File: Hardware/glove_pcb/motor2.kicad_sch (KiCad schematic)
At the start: 22 parts, among them J8 Conn_01x02, U12 DRV8876PWPR

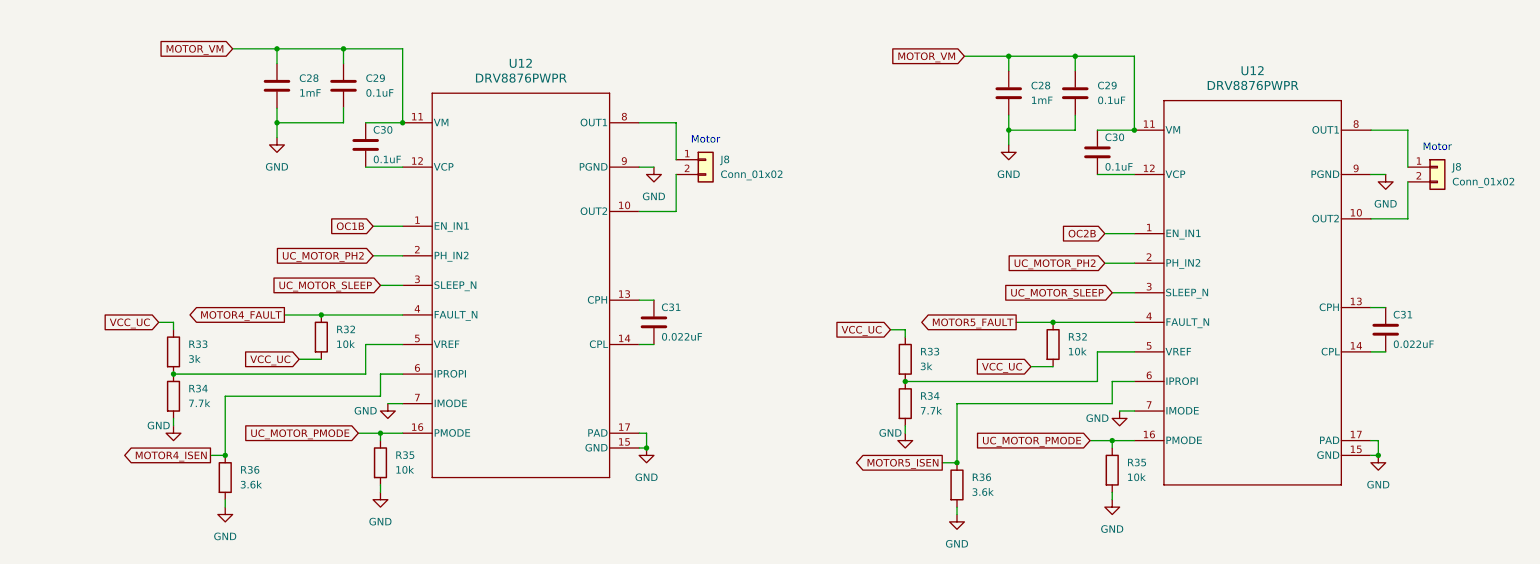
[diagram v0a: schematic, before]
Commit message: Add titles to pages and reannotate
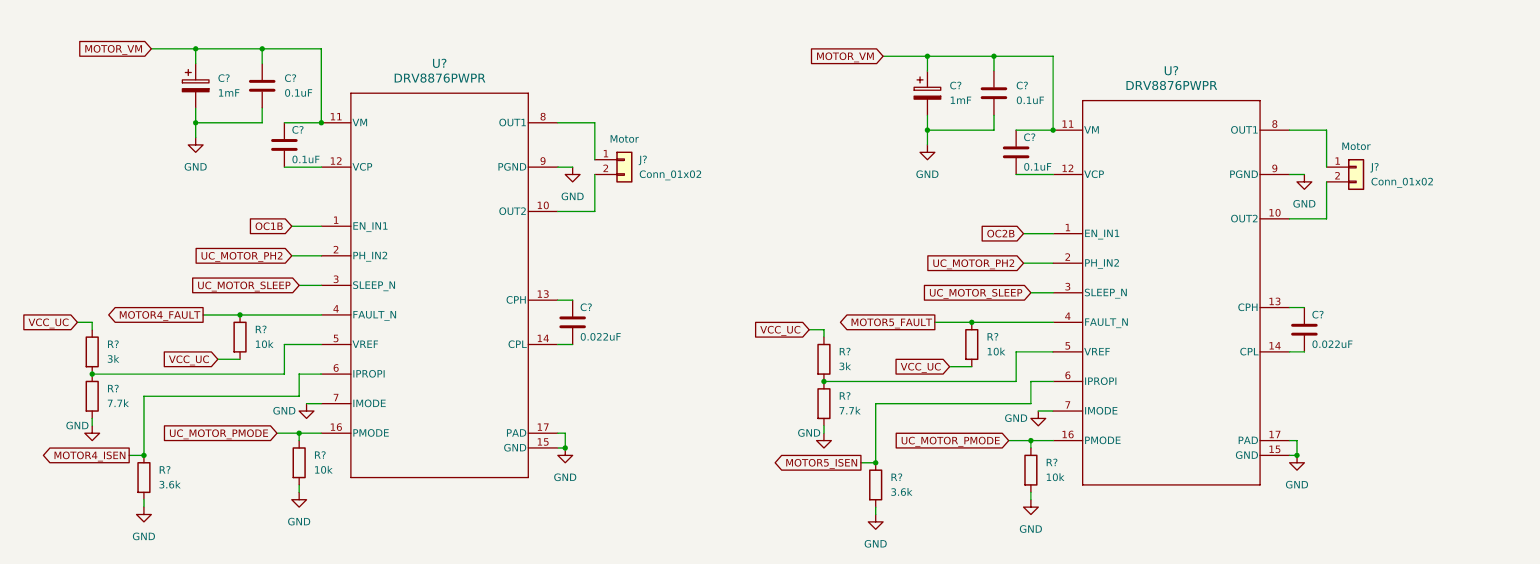
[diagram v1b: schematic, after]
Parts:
- C? (x2): renamed from C28; symbol Device:C -> Device:C_Polarized
- renumbered C30 to C?, C29 to C?, C31 to C?, J8 to J?, R36 to R?, R35 to R?, R34 to R?, R32 to R?, R33 to R?, U12 to U?
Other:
- company: (none) -> COEN 490 Team 15
- title: (none) -> Motor Drivers (2/2)
- moved on the sheet: C?, J?, R?, U?

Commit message: Finalize schematic for real this time
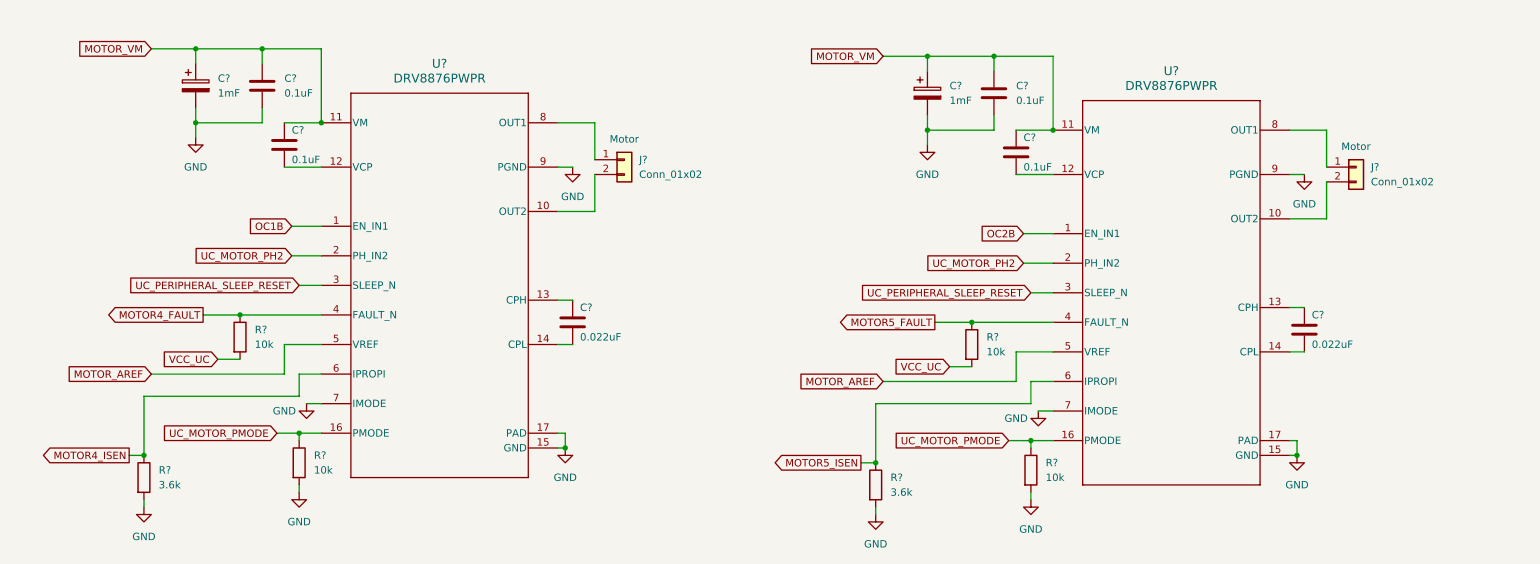
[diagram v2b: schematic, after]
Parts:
- removed R? (x2): 7.7k, symbol Device:R
- removed R? (x2): 3k, symbol Device:R
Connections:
- net MOTOR_AREF: now reaches U?.5 (VREF)
- net MOTOR_AREF: now also U?.5 (VREF)
- net UC_MOTOR_SLEEP renamed UC_PERIPHERAL_SLEEP_RESET

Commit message: Added Footprints
I Added footprints for every components in PCB
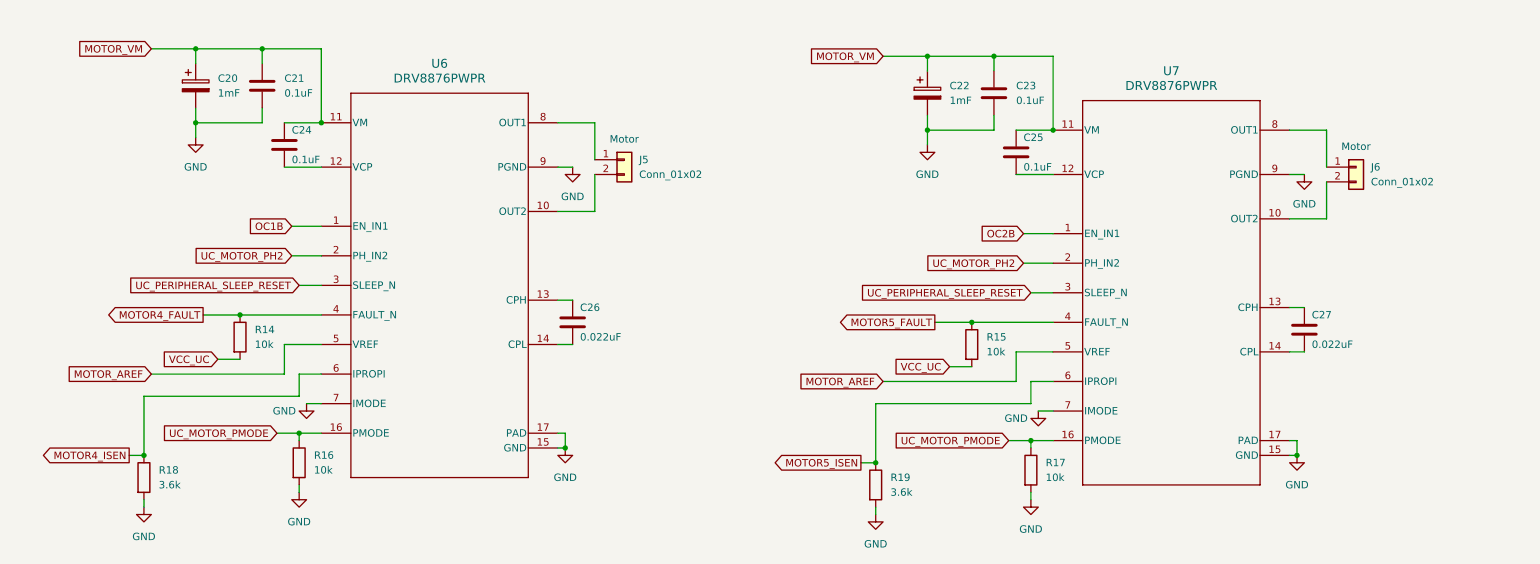
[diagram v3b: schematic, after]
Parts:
- C20, C22: renamed from C?; footprint (none) -> Capacitor_THT:CP_Radial_D10.0mm_P5.00mm
- C21, C23, C24, C25, C26, C27: renamed from C?; footprint (none) -> Capacitor_SMD:C_0603_1608Metric_Pad1.08x0.95mm_HandSolder
- J5, J6: renamed from J?; footprint (none) -> Connector_Molex:Molex_Micro-Fit_3.0_43650-0215_1x02_P3.00mm_Vertical
- R14, R15, R16, R17, R18, R19: renamed from R?; footprint (none) -> Resistor_SMD:R_0805_2012Metric_Pad1.20x1.40mm_HandSolder
- gave numbers to parts that had none: 2

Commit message: Made most of changes from meeting
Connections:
- net MOTOR_VM renamed +12V
- net VCC_UC renamed +5V
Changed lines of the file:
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@@
-    )
-  )
-  (global_label "VCC_UC" (shape input) (at 179.07 82.55 180) (fields_autoplaced)
-    (effects (font (size 1.27 1.27)) (justify right))
-    (property "Intersheetrefs" "${INTERSHEET_REFS}" (at 168.8881 82.55 0)
-      (effects (font (size 1.27 1.27)) (justify right) hide)
     )
   )
@@
     )
   )
-  (global_label "MOTOR_VM" (shape input) (at 41.91 27.94 180) (fields_autoplaced)
-    (effects (font (size 1.27 1.27)) (justify right))
-    (property "Intersheetrefs" "${INTERSHEET_REFS}" (at 29.0672 27.94 0)
-      (effects (font (size 1.27 1.27)) (justify right) hide)
-    )
-  )
   (global_label "UC_MOTOR_PH2" (shape input) (at 191.77 64.77 180) (fields_autoplaced)
     (effects (font (size 1.27 1.27)) (justify right))
@@
     )
   )
-  (global_label "MOTOR_VM" (shape input) (at 167.64 29.21 180) (fields_autoplaced)
-    (effects (font (size 1.27 1.27)) (justify right))
-    (property "Intersheetrefs" "${INTERSHEET_REFS}" (at 154.7972 29.21 0)
-      (effects (font (size 1.27 1.27)) (justify right) hide)
-    )
-  )
-  (global_label "VCC_UC" (shape input) (at 53.34 81.28 180) (fields_autoplaced)
-    (effects (font (size 1.27 1.27)) (justify right))
-    (property "Intersheetrefs" "${INTERSHEET_REFS}" (at 43.1581 81.28 0)
-      (effects (font (size 1.27 1.27)) (justify right) hide)
-    )
-  )
   (global_label "OC2B" (shape input) (at 191.77 59.69 180) (fields_autoplaced)
     (effects (font (size 1.27 1.27)) (justify right))
@@
         (path "/747ff5f3-d342-40b0-8e4e-75b3a3063e75/244d4343-af6d-4477-97fd-05de712328be"
           (reference "J5") (unit 1)
+        )
+      )
+    )
+  )
+  (symbol (lib_id "power:+12V") (at 167.64 29.21 0) (unit 1)
+    (in_bom yes) (on_board yes) (dnp no) (fields_autoplaced)
+    (property "Reference" "#PWR078" (at 167.64 33.02 0)
+      (effects (font (size 1.27 1.27)) hide)
+    )
+    (property "Value" "+12V" (at 167.64 24.13 0)
+      (effects (font (size 1.27 1.27)))
+    )
+    (property "Footprint" "" (at 167.64 29.21 0)
+      (effects (font (size 1.27 1.27)) hide)
+    )
+    (property "Datasheet" "" (at 167.64 29.21 0)
+      (effects (font (size 1.27 1.27)) hide)
+    )
+    (pin "1")
+    (instances
+      (project "glove_pcb"
+        (path "/747ff5f3-d342-40b0-8e4e-75b3a3063e75/244d4343-af6d-4477-97fd-05de712328be"
+          (reference "#PWR078") (unit 1)
         )
       )
@@
     )
   )
+  (symbol (lib_id "power:+5V") (at 179.07 82.55 0) (unit 1)
+    (in_bom yes) (on_board yes) (dnp no)
+    (property "Reference" "#PWR083" (at 179.07 86.36 0)
+      (effects (font (size 1.27 1.27)) hide)
+    )
+    (property "Value" "+5V" (at 179.07 78.74 0)
+      (effects (font (size 1.27 1.27)))
+    )
+    (property "Footprint" "" (at 179.07 82.55 0)
+      (effects (font (size 1.27 1.27)) hide)
+    )
+    (property "Datasheet" "" (at 179.07 82.55 0)
+      (effects (font (size 1.27 1.27)) hide)
+    )
+    (pin "1")
+    (instances
+      (project "glove_pcb"
+        (path "/747ff5f3-d342-40b0-8e4e-75b3a3063e75/244d4343-af6d-4477-97fd-05de712328be"
+          (reference "#PWR083") (unit 1)
+        )
+      )
+    )
+  )
   (symbol (lib_id "Device:C") (at 186.69 35.56 0) (unit 1)
     (in_bom yes) (on_board yes) (dnp no) (fields_autoplaced)
@@
     )
   )
+  (symbol (lib_id "power:+5V") (at 53.34 81.28 0) (unit 1)
+    (in_bom yes) (on_board yes) (dnp no)
+    (property "Reference" "#PWR082" (at 53.34 85.09 0)
+      (effects (font (size 1.27 1.27)) hide)
+    )
+    (property "Value" "+5V" (at 53.34 77.47 0)
+      (effects (font (size 1.27 1.27)))
+    )
+    (property "Footprint" "" (at 53.34 81.28 0)
+      (effects (font (size 1.27 1.27)) hide)
+    )
+    (property "Datasheet" "" (at 53.34 81.28 0)
+      (effects (font (size 1.27 1.27)) hide)
+    )
+    (pin "1")
+    (instances
+      (project "glove_pcb"
+        (path "/747ff5f3-d342-40b0-8e4e-75b3a3063e75/244d4343-af6d-4477-97fd-05de712328be"
+          (reference "#PWR082") (unit 1)
+        )
+      )
+    )
+  )
   (symbol (lib_id "power:GND") (at 166.37 107.95 0) (unit 1)
     (in_bom yes) (on_board yes) (dnp no) (fields_autoplaced)
@@
         )
       )
+    )
+  )
+  (symbol (lib_id "power:+12V") (at 41.91 27.94 0) (unit 1)
+    (in_bom yes) (on_board yes) (dnp no) (fields_autoplaced)
+    (property "Reference" "#PWR077" (at 41.91 31.75 0)
+      (effects (font (size 1.27 1.27)) hide)
+    )
+    (property "Value" "+12V" (at 41.91 22.86 0)
+      (effects (font (size 1.27 1.27)))
+    )
+    (property "Footprint" "" (at 41.91 27.94 0)
+      (effects (font (size 1.27 1.27)) hide)
+    )
+    (property "Datasheet" "" (at 41.91 27.94 0)
+      (effects (font (size 1.27 1.27)) hide)
+    )
+    (pin "1")
+    (instances
+      (project "glove_pcb"
+        (path "/747ff5f3-d342-40b0-8e4e-75b3a3063e75/244d4343-af6d-4477-97fd-05de712328be"
+          (reference "#PWR077") (unit 1)
+        )
+      )

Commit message: Finish changes according to feedback
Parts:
- removed R16, R17: 10k, Resistor_SMD:R_0805_2012Metric_Pad1.20x1.40mm_HandSolder, symbol Device:R
- renumbered C20 to C22, C21 to C23, C22 to C24, C23 to C25, C24 to C26, C25 to C27, C26 to C28, C27 to C29, R14 to R12, R15 to R13, R18 to R14, R19 to R15
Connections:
- net UC_MOTOR_PMODE is gone; now on net GND: U6.16 (PMODE), U7.16 (PMODE)

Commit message: Finish schematic updates
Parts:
- C22, C24: value 1mF -> 1000uF
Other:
- moved on the sheet: C22, C24
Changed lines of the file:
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@@
   (junction (at 60.96 27.94) (diameter 0) (color 0 0 0 0)
   )
+  (junction (at 172.72 41.91) (diameter 0) (color 0 0 0 0)
+  )
   (junction (at 195.58 95.25) (diameter 0) (color 0 0 0 0)
   )
   (junction (at 113.03 96.52) (diameter 0) (color 0 0 0 0)
   )
-  (junction (at 175.26 41.91) (diameter 0) (color 0 0 0 0)
-  )
   (junction (at 166.37 99.06) (diameter 0) (color 0 0 0 0)
   )
@@
   (junction (at 40.64 97.79) (diameter 0) (color 0 0 0 0)
   )
-  (junction (at 49.53 27.94) (diameter 0) (color 0 0 0 0)
-  )
-  (junction (at 49.53 40.64) (diameter 0) (color 0 0 0 0)
+  (junction (at 46.99 27.94) (diameter 0) (color 0 0 0 0)
+  )
+  (junction (at 46.99 40.64) (diameter 0) (color 0 0 0 0)
+  )
+  (junction (at 172.72 29.21) (diameter 0) (color 0 0 0 0)
   )
   (junction (at 57.15 73.66) (diameter 0) (color 0 0 0 0)
@@
   (junction (at 182.88 74.93) (diameter 0) (color 0 0 0 0)
   )
-  (junction (at 175.26 29.21) (diameter 0) (color 0 0 0 0)
-  )
   (junction (at 186.69 29.21) (diameter 0) (color 0 0 0 0)
   )
@@
     (stroke (width 0) (type default))
   )
-  (wire (pts (xy 49.53 40.64) (xy 49.53 43.18))
+  (wire (pts (xy 46.99 40.64) (xy 60.96 40.64))
+    (stroke (width 0) (type default))
+  )
+  (wire (pts (xy 46.99 40.64) (xy 46.99 43.18))
     (stroke (width 0) (type default))
   )
@@
     (stroke (width 0) (type default))
   )
-  (wire (pts (xy 175.26 41.91) (xy 186.69 41.91))
-    (stroke (width 0) (type default))
-  )
   (wire (pts (xy 67.31 83.82) (xy 67.31 87.63))
     (stroke (width 0) (type default))
@@
     (stroke (width 0) (type default))
   )
-  (wire (pts (xy 175.26 41.91) (xy 175.26 44.45))
+  (wire (pts (xy 172.72 41.91) (xy 172.72 44.45))
     (stroke (width 0) (type default))
   )
@@
     (stroke (width 0) (type default))
   )
-  (wire (pts (xy 167.64 29.21) (xy 175.26 29.21))
+  (wire (pts (xy 167.64 29.21) (xy 172.72 29.21))
     (stroke (width 0) (type default))
   )
@@
     (stroke (width 0) (type default))
   )
-  (wire (pts (xy 49.53 40.64) (xy 60.96 40.64))
-    (stroke (width 0) (type default))
-  )
   (wire (pts (xy 118.11 55.88) (xy 118.11 49.53))
     (stroke (width 0) (type default))
@@
     (stroke (width 0) (type default))
   )
+  (wire (pts (xy 172.72 29.21) (xy 186.69 29.21))
+    (stroke (width 0) (type default))
+  )
   (wire (pts (xy 191.77 59.69) (xy 196.85 59.69))
     (stroke (width 0) (type default))
@@
     (stroke (width 0) (type default))
   )
-  (wire (pts (xy 60.96 27.94) (xy 49.53 27.94))
+  (wire (pts (xy 46.99 27.94) (xy 60.96 27.94))
     (stroke (width 0) (type default))
   )
@@
     (stroke (width 0) (type default))
   )
-  (wire (pts (xy 175.26 39.37) (xy 175.26 41.91))
+  (wire (pts (xy 172.72 39.37) (xy 172.72 41.91))
     (stroke (width 0) (type default))
   )
@@
     (stroke (width 0) (type default))
   )
+  (wire (pts (xy 172.72 41.91) (xy 186.69 41.91))
+    (stroke (width 0) (type default))
+  )
   (wire (pts (xy 53.34 81.28) (xy 57.15 81.28))
     (stroke (width 0) (type default))
@@
     (stroke (width 0) (type default))
   )
-  (wire (pts (xy 186.69 29.21) (xy 175.26 29.21))
-    (stroke (width 0) (type default))
-  )
   (wire (pts (xy 38.1 97.79) (xy 40.64 97.79))
     (stroke (width 0) (type default))
@@
     (stroke (width 0) (type default))
   )
-  (wire (pts (xy 49.53 27.94) (xy 49.53 30.48))
+  (wire (pts (xy 46.99 27.94) (xy 46.99 30.48))
     (stroke (width 0) (type default))
   )
@@
     (stroke (width 0) (type default))
   )
-  (wire (pts (xy 41.91 27.94) (xy 49.53 27.94))
+  (wire (pts (xy 41.91 27.94) (xy 46.99 27.94))
     (stroke (width 0) (type default))
   )
@@
     (stroke (width 0) (type default))
   )
-  (wire (pts (xy 49.53 38.1) (xy 49.53 40.64))
+  (wire (pts (xy 46.99 38.1) (xy 46.99 40.64))
     (stroke (width 0) (type default))
   )
@@
     (stroke (width 0) (type default))
   )
-  (wire (pts (xy 175.26 29.21) (xy 175.26 31.75))
+  (wire (pts (xy 172.72 29.21) (xy 172.72 31.75))
     (stroke (width 0) (type default))
   )
@@
     )
   )
-  (symbol (lib_id "Device:C_Polarized") (at 49.53 34.29 0) (unit 1)
+  (symbol (lib_id "Device:C_Polarized") (at 46.99 34.29 0) (unit 1)
     (in_bom yes) (on_board yes) (dnp no)
-    (property "Reference" "C22" (at 53.34 33.02 0)
-      (effects (font (size 1.27 1.27)) (justify left))
-    )
-    (property "Value" "1mF" (at 53.34 35.56 0)
-      (effects (font (size 1.27 1.27)) (justify left))
-    )
-    (property "Footprint" "Capacitor_THT:CP_Radial_D10.0mm_P5.00mm" (at 50.4952 38.1 0)
-      (effects (font (size 1.27 1.27)) hide)
-    )
-    (property "Datasheet" "~" (at 49.53 34.29 0)
+    (property "Reference" "C22" (at 50.8 33.02 0)
+      (effects (font (size 1.27 1.27)) (justify left))
+    )
+    (property "Value" "1000uF" (at 50.8 35.56 0)
+      (effects (font (size 1.27 1.27)) (justify left))
+    )
+    (property "Footprint" "Capacitor_THT:CP_Radial_D10.0mm_P5.00mm" (at 47.9552 38.1 0)
+      (effects (font (size 1.27 1.27)) hide)
+    )
+    (property "Datasheet" "~" (at 46.99 34.29 0)
       (effects (font (size 1.27 1.27)) hide)
     )
@@
     )
   )
-  (symbol (lib_id "power:GND") (at 175.26 44.45 0) (unit 1)
-    (in_bom yes) (on_board yes) (dnp no) (fields_autoplaced)
-    (property "Reference" "#PWR041" (at 175.26 50.8 0)
-      (effects (font (size 1.27 1.27)) hide)
-    )
-    (property "Value" "GND" (at 175.26 49.53 0)
+  (symbol (lib_id "power:GND") (at 172.72 44.45 0) (unit 1)
+    (in_bom yes) (on_board yes) (dnp no) (fields_autoplaced)
+    (property "Reference" "#PWR041" (at 172.72 50.8 0)
+      (effects (font (size 1.27 1.27)) hide)
+    )
+    (property "Value" "GND" (at 172.72 49.53 0)
       (effects (font (size 1.27 1.27)))
     )
-    (property "Footprint" "" (at 175.26 44.45 0)
-      (effects (font (size 1.27 1.27)) hide)
-    )
-    (property "Datasheet" "" (at 175.26 44.45 0)
+    (property "Footprint" "" (at 172.72 44.45 0)
+      (effects (font (size 1.27 1.27)) hide)
+    )
+    (property "Datasheet" "" (at 172.72 44.45 0)
       (effects (font (size 1.27 1.27)) hide)
     )
@@
     )
   )
-  (symbol (lib_id "Device:C_Polarized") (at 175.26 35.56 0) (unit 1)
+  (symbol (lib_id "Device:C_Polarized") (at 172.72 35.56 0) (unit 1)
     (in_bom yes) (on_board yes) (dnp no)
-    (property "Reference" "C24" (at 179.07 34.29 0)
-      (effects (font (size 1.27 1.27)) (justify left))
-    )
-    (property "Value" "1mF" (at 179.07 36.83 0)
-      (effects (font (size 1.27 1.27)) (justify left))
-    )
-    (property "Footprint" "Capacitor_THT:CP_Radial_D10.0mm_P5.00mm" (at 176.2252 39.37 0)
-      (effects (font (size 1.27 1.27)) hide)
-    )
-    (property "Datasheet" "~" (at 175.26 35.56 0)
+    (property "Reference" "C24" (at 176.53 34.29 0)
+      (effects (font (size 1.27 1.27)) (justify left))
+    )
+    (property "Value" "1000uF" (at 176.53 36.83 0)
+      (effects (font (size 1.27 1.27)) (justify left))
+    )
+    (property "Footprint" "Capacitor_THT:CP_Radial_D10.0mm_P5.00mm" (at 173.6852 39.37 0)
+      (effects (font (size 1.27 1.27)) hide)
+    )
+    (property "Datasheet" "~" (at 172.72 35.56 0)
       (effects (font (size 1.27 1.27)) hide)
     )
@@
     )
   )
-  (symbol (lib_id "power:GND") (at 49.53 43.18 0) (unit 1)
-    (in_bom yes) (on_board yes) (dnp no) (fields_autoplaced)
-    (property "Reference" "#PWR040" (at 49.53 49.53 0)
-      (effects (font (size 1.27 1.27)) hide)
-    )
-    (property "Value" "GND" (at 49.53 48.26 0)
+  (symbol (lib_id "power:GND") (at 46.99 43.18 0) (unit 1)
+    (in_bom yes) (on_board yes) (dnp no) (fields_autoplaced)
+    (property "Reference" "#PWR040" (at 46.99 49.53 0)
+      (effects (font (size 1.27 1.27)) hide)
+    )
+    (property "Value" "GND" (at 46.99 48.26 0)
       (effects (font (size 1.27 1.27)))
     )
-    (property "Footprint" "" (at 49.53 43.18 0)
-      (effects (font (size 1.27 1.27)) hide)
-    )
-    (property "Datasheet" "" (at 49.53 43.18 0)
-      (effects (font (size 1.27 1.27)) hide)
-    )
+    (property "Footprint" "" (at 46.99 43.18 0)
+      (effects (font (size 1.27 1.27)) hide)
+    )
+    (property "Datasheet" "" (at 46.99 43.18 0)
+      (effects (font (size 1.27 1.27)) hide)
+    )
